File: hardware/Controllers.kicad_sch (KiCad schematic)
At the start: 1 part

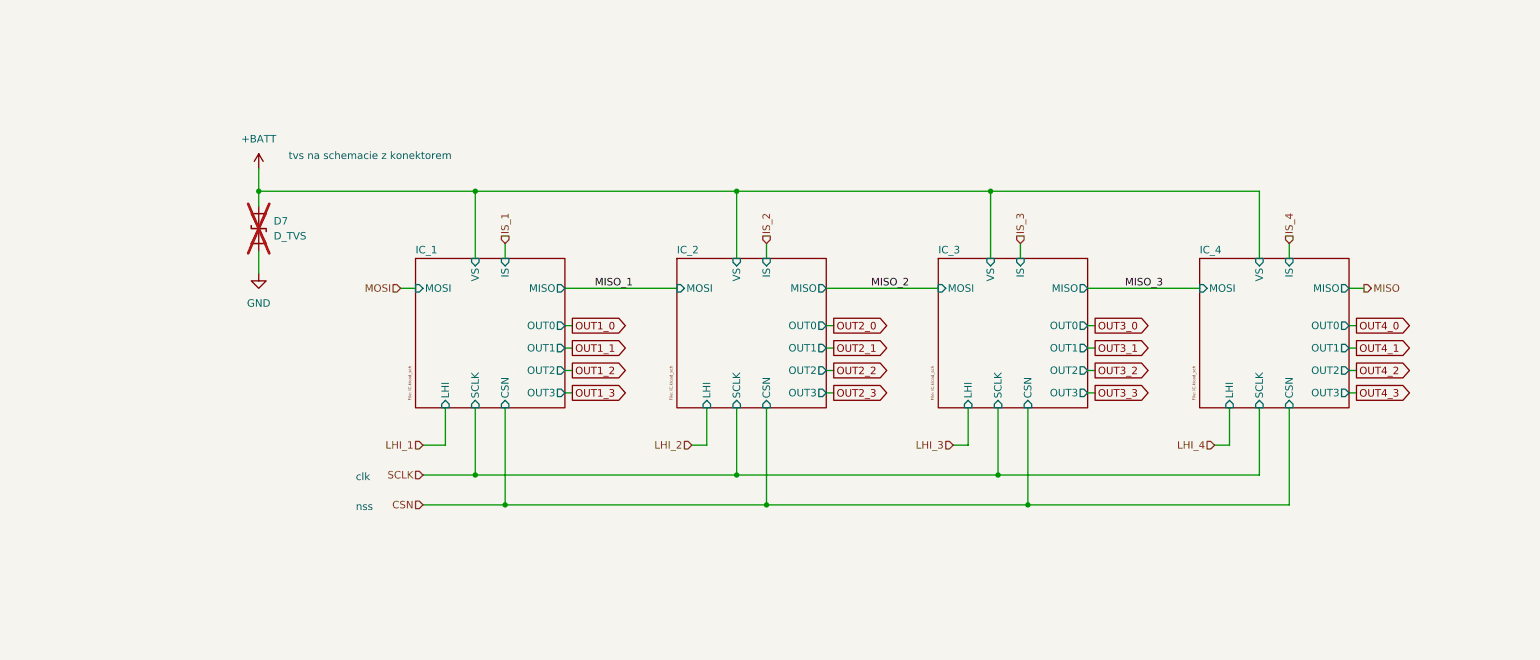
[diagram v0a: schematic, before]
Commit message: cube->cmake port, current calc fix, spi datalength fix, hard-v1.1.0 sync
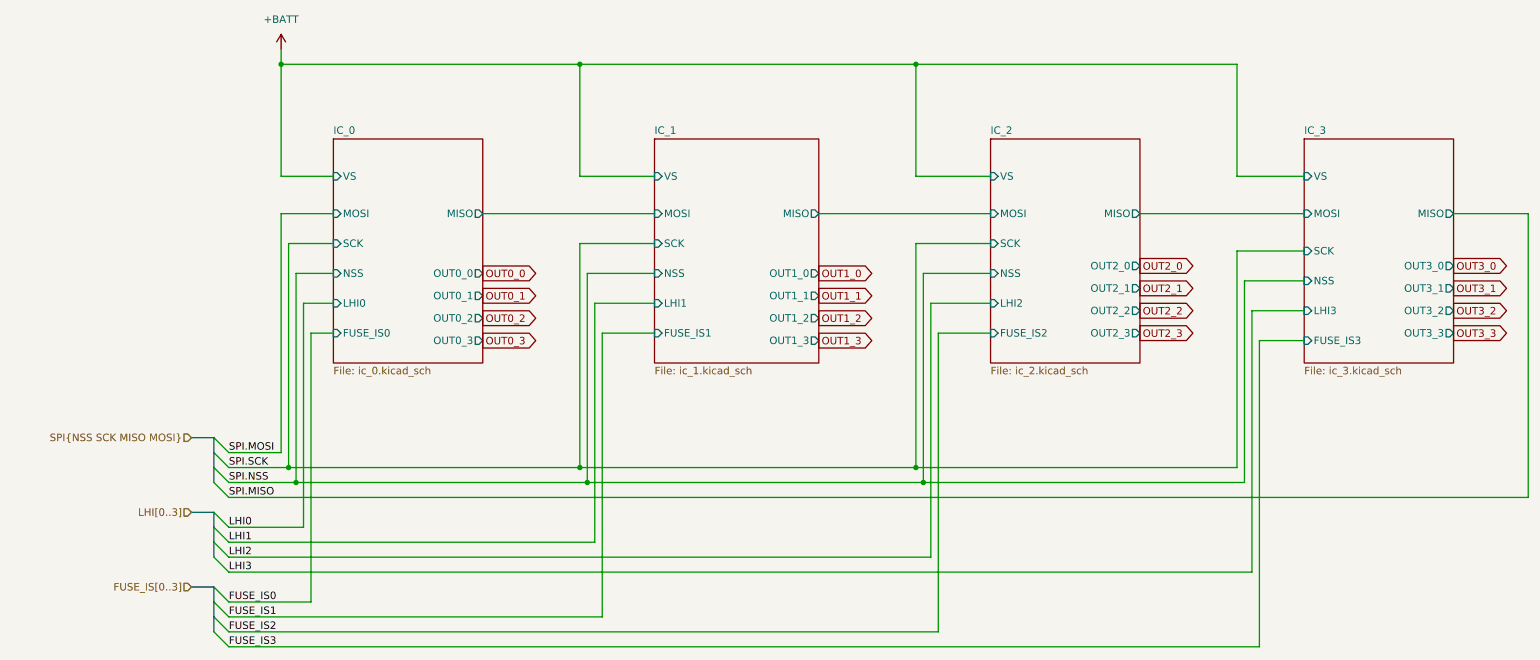
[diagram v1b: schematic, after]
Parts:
- removed D7: D_TVS, symbol Device:D_TVS
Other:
- removed sheet IC_4
- added sheet IC_0 (ic_0.kicad_sch)
- sheet IC_1: file IC.kicad_sch -> ic_1.kicad_sch
- sheet IC_1 ports: added FUSE_IS1, LHI1, NSS, OUT1_0, OUT1_1, OUT1_2, OUT1_3, SCK; removed CSN, IS, LHI, OUT0, OUT1, OUT2, OUT3, SCLK
- sheet IC_2: file IC.kicad_sch -> ic_2.kicad_sch
- sheet IC_2 ports: added FUSE_IS2, LHI2, NSS, OUT2_0, OUT2_1, OUT2_2, OUT2_3, SCK; removed CSN, IS, LHI, OUT0, OUT1, OUT2, OUT3, SCLK
- sheet IC_3: file IC.kicad_sch -> ic_3.kicad_sch
- sheet IC_3 ports: added FUSE_IS3, LHI3, NSS, OUT3_0, OUT3_1, OUT3_2, OUT3_3, SCK; removed CSN, IS, LHI, OUT0, OUT1, OUT2, OUT3, SCLK
- note removed: "clk"
- note removed: "nss"
- note removed: "tvs na schemacie z konektorem"
- company: (none) -> Authors: Grzegorz Potocki Jędrzej Kasprzyk
- title: (none) -> PDUv3
